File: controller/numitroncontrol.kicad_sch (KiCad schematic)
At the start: 9 parts, among them J0 Screw_Terminal_01x02, J1 Conn_01x06, J2 Conn_01x06, J3 RTC, J4 Screw_Terminal_01x03, U1 LM317_TO-220

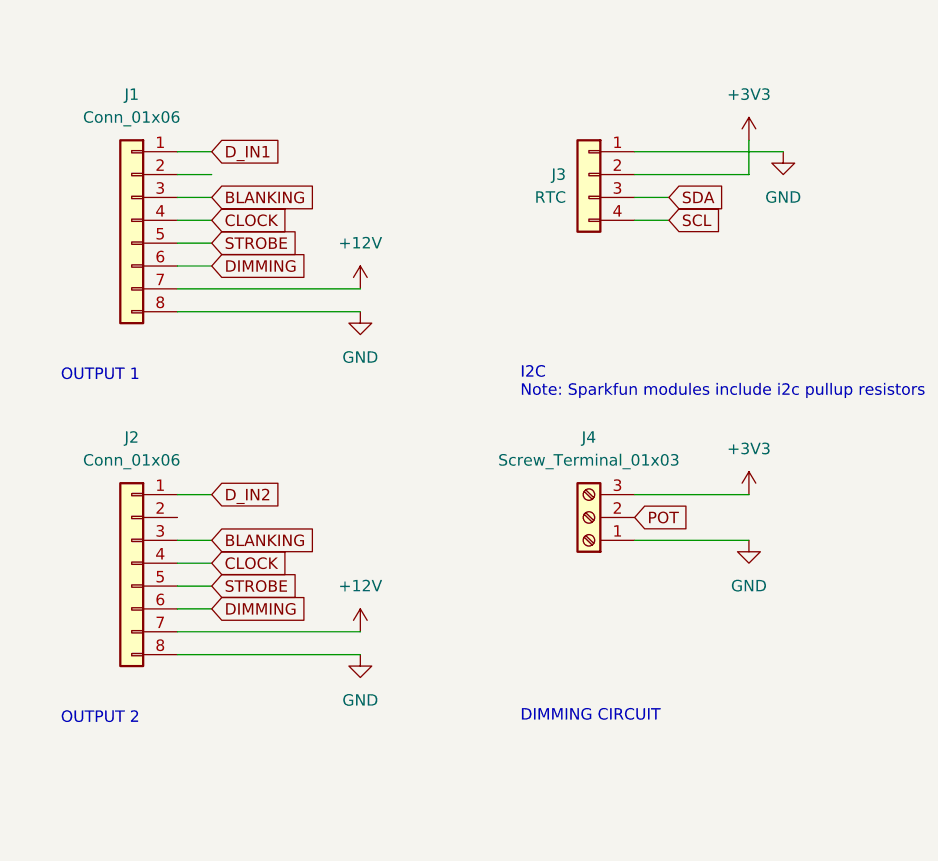
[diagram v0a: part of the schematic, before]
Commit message: Added jumper for control schemes
can have discrete or daisy control of second output on control board
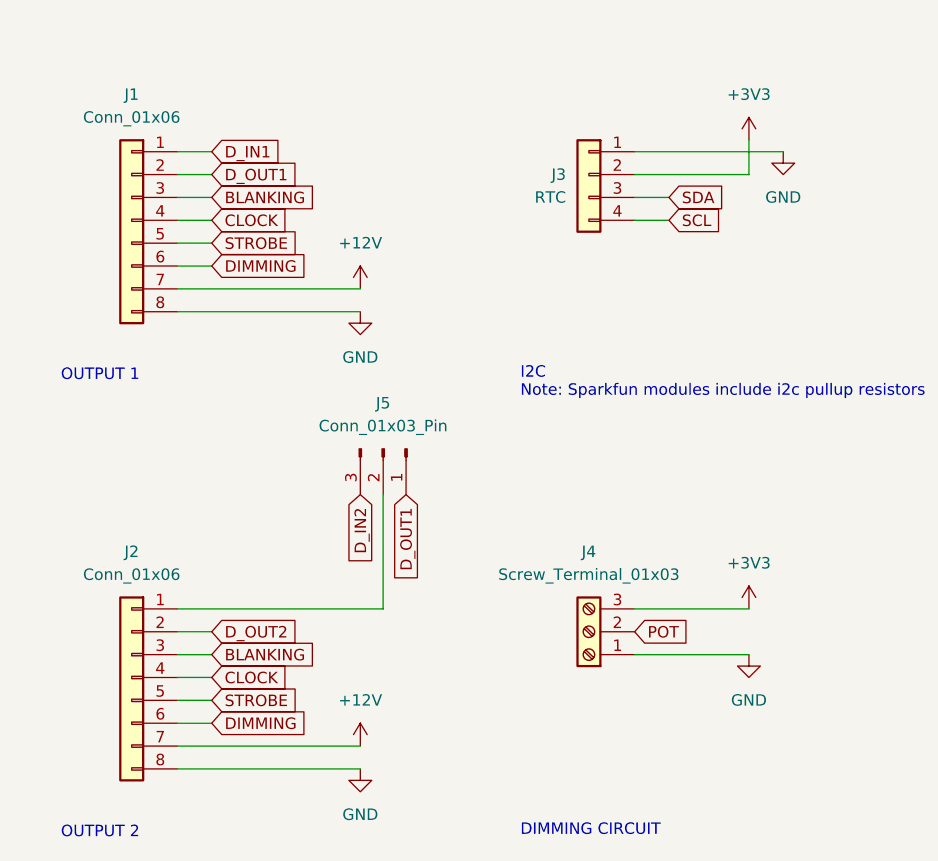
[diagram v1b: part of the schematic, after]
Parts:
- added J5: Conn_01x03_Pin, Connector_PinSocket_2.54mm:PinSocket_1x03_P2.54mm_Vertical, symbol Connector:Conn_01x03_Pin
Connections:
- net D_IN2: now also J5.3 (Pin_3); no longer J2.1 (Pin_1)
- net D_OUT1: now reaches J1.2 (Pin_2)
- net D_OUT1: now also J5.1 (Pin_1)
- net D_OUT2: now reaches J2.2 (Pin_2)
- new net: J2.1 (Pin_1), J5.2 (Pin_2)
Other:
- moved on the sheet: J2, J4

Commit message: control board layout tweaks
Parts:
- J3: symbol Connector_Generic:Conn_01x04 -> Connector:Screw_Terminal_01x04
- J4: footprint TerminalBlock_4Ucon:TerminalBlock_4Ucon_1x03_P3.50mm_Horizontal -> Connector_PinHeader_2.54mm:PinHeader_1x03_P2.54mm_Vertical
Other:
- moved on the sheet: J5
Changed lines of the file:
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@@
+	(wire
+		(pts
+			(xy 31.75 40.64) (xy 25.4 40.64)
+		)
+		(stroke
+			(width 0)
+			(type default)
+		)
+	)
+	(wire
+		(pts
+			(xy 114.3 85.09) (xy 114.3 86.36)
+		)
+		(stroke
+			(width 0)
+			(type default)
+		)
+	)
+	(wire
+		(pts
+			(xy 25.4 38.1) (xy 36.83 38.1)
+		)
+		(stroke
+			(width 0)
+			(type default)
+		)
+	)
+	(wire
+		(pts
+			(xy 48.26 177.8) (xy 48.26 170.18)
+		)
+		(stroke
+			(width 0)
+			(type default)
+		)
+	)
+	(wire
+		(pts
+			(xy 63.5 53.34) (xy 63.5 50.8)
+		)
+		(stroke
+			(width 0)
+			(type default)
+		)
+	)
+	(wire
+		(pts
+			(xy 44.45 50.8) (xy 63.5 50.8)
+		)
+		(stroke
+			(width 0)
+			(type default)
+		)
+	)
+	(wire
+		(pts
+			(xy 25.4 180.34) (xy 29.21 180.34)
+		)
+		(stroke
+			(width 0)
+			(type default)
+		)
+	)
+	(wire
+		(pts
+			(xy 88.9 129.54) (xy 76.2 129.54)
+		)
+		(stroke
+			(width 0)
+			(type default)
+		)
+	)
+	(wire
+		(pts
+			(xy 177.8 63.5) (xy 180.34 63.5)
+		)
+		(stroke
+			(width 0)
+			(type default)
+		)
+	)
+	(wire
+		(pts
+			(xy 123.19 68.58) (xy 127 68.58)
+		)
+		(stroke
+			(width 0)
+			(type default)
+		)
+	)
+	(wire
+		(pts
+			(xy 88.9 125.73) (xy 88.9 129.54)
+		)
+		(stroke
+			(width 0)
+			(type default)
+		)
+	)
+	(wire
+		(pts
+			(xy 25.4 190.5) (xy 29.21 190.5)
+		)
+		(stroke
+			(width 0)
+			(type default)
+		)
+	)
+	(wire
+		(pts
+			(xy 31.75 40.64) (xy 31.75 63.5)
+		)
+		(stroke
+			(width 0)
+			(type default)
+		)
+	)
+	(wire
+		(pts
+			(xy 63.5 63.5) (xy 63.5 60.96)
+		)
+		(stroke
+			(width 0)
+			(type default)
+		)
+	)
+	(wire
+		(pts
+			(xy 114.3 101.6) (xy 114.3 96.52)
+		)
+		(stroke
+			(width 0)
+			(type default)
+		)
+	)
+	(wire
+		(pts
+			(xy 25.4 185.42) (xy 29.21 185.42)
+		)
+		(stroke
+			(width 0)
+			(type default)
+		)
+	)
+	(wire
+		(pts
+			(xy 177.8 66.04) (xy 180.34 66.04)
+		)
+		(stroke
+			(width 0)
+			(type default)
+		)
+	)
+	(wire
+		(pts
+			(xy 25.4 139.7) (xy 29.21 139.7)
+		)
+		(stroke
+			(width 0)
+			(type default)
+		)
+	)
+	(wire
+		(pts
+			(xy 88.9 177.8) (xy 76.2 177.8)
+		)
+		(stroke
+			(width 0)
+			(type default)
+		)
+	)
+	(wire
+		(pts
+			(xy 25.4 129.54) (xy 29.21 129.54)
+		)
+		(stroke
+			(width 0)
+			(type default)
+		)
+	)
+	(wire
+		(pts
+			(xy 106.68 91.44) (xy 127 91.44)
+		)
+		(stroke
+			(width 0)
+			(type default)
+		)
+	)
 	(wire
 		(pts
 			(xy 25.4 177.8) (xy 48.26 177.8)
-		)
-		(stroke
-			(width 0)
-			(type default)
-		)
-	)
-	(wire
-		(pts
-			(xy 31.75 40.64) (xy 25.4 40.64)
-		)
-		(stroke
-			(width 0)
-			(type default)
-		)
-	)
-	(wire
-		(pts
-			(xy 114.3 85.09) (xy 114.3 86.36)
-		)
-		(stroke
-			(width 0)
-			(type default)
-		)
-	)
-	(wire
-		(pts
-			(xy 25.4 38.1) (xy 36.83 38.1)
-		)
-		(stroke
-			(width 0)
-			(type default)
-		)
-	)
-	(wire
-		(pts
-			(xy 48.26 177.8) (xy 48.26 165.1)
-		)
-		(stroke
-			(width 0)
-			(type default)
-		)
-	)
-	(wire
-		(pts
-			(xy 63.5 53.34) (xy 63.5 50.8)
-		)
-		(stroke
-			(width 0)
-			(type default)
-		)
-	)
-	(wire
-		(pts
-			(xy 44.45 50.8) (xy 63.5 50.8)
-		)
-		(stroke
-			(width 0)
-			(type default)
-		)
-	)
-	(wire
-		(pts
-			(xy 25.4 180.34) (xy 29.21 180.34)
-		)
-		(stroke
-			(width 0)
-			(type default)
-		)
-	)
-	(wire
-		(pts
-			(xy 88.9 129.54) (xy 76.2 129.54)
-		)
-		(stroke
-			(width 0)
-			(type default)
-		)
-	)
-	(wire
-		(pts
-			(xy 177.8 63.5) (xy 180.34 63.5)
-		)
-		(stroke
-			(width 0)
-			(type default)
-		)
-	)
-	(wire
-		(pts
-			(xy 123.19 68.58) (xy 127 68.58)
-		)
-		(stroke
-			(width 0)
-			(type default)
-		)
-	)
-	(wire
-		(pts
-			(xy 88.9 125.73) (xy 88.9 129.54)
-		)
-		(stroke
-			(width 0)
-			(type default)
-		)
-	)
-	(wire
-		(pts
-			(xy 25.4 190.5) (xy 29.21 190.5)
-		)
-		(stroke
-			(width 0)
-			(type default)
-		)
-	)
-	(wire
-		(pts
-			(xy 31.75 40.64) (xy 31.75 63.5)
-		)
-		(stroke
-			(width 0)
-			(type default)
-		)
-	)
-	(wire
-		(pts
-			(xy 63.5 63.5) (xy 63.5 60.96)
-		)
-		(stroke
-			(width 0)
-			(type default)
-		)
-	)
-	(wire
-		(pts
-			(xy 114.3 101.6) (xy 114.3 96.52)
-		)
-		(stroke
-			(width 0)
-			(type default)
-		)
-	)
-	(wire
-		(pts
-			(xy 25.4 185.42) (xy 29.21 185.42)
-		)
-		(stroke
-			(width 0)
-			(type default)
-		)
-	)
-	(wire
-		(pts
-			(xy 177.8 66.04) (xy 180.34 66.04)
-		)
-		(stroke
-			(width 0)
-			(type default)
-		)
-	)
-	(wire
-		(pts
-			(xy 25.4 139.7) (xy 29.21 139.7)
-		)
-		(stroke
-			(width 0)
-			(type default)
-		)
-	)
-	(wire
-		(pts
-			(xy 88.9 177.8) (xy 76.2 177.8)
-		)
-		(stroke
-			(width 0)
-			(type default)
-		)
-	)
-	(wire
-		(pts
-			(xy 25.4 129.54) (xy 29.21 129.54)
-		)
-		(stroke
-			(width 0)
-			(type default)
-		)
-	)
-	(wire
-		(pts
-			(xy 106.68 91.44) (xy 127 91.44)
 		)
 		(stroke
@@
 	(global_label "D_OUT1"
 		(shape input)
-		(at 50.8 165.1 270)
+		(at 50.8 170.18 270)
 		(fields_autoplaced yes)
 		(effects
@@
 		)
 		(property "Intersheetrefs" "${INTERSHEET_REFS}"
-			(at 50.8 175.1609 90)
+			(at 50.8 180.2409 90)
 			(effects
 				(font
@@
 	(global_label "D_IN2"
 		(shape input)
-		(at 45.72 165.1 270)
+		(at 45.72 170.18 270)
 		(fields_autoplaced yes)
 		(effects
@@
 		)
 		(property "Intersheetrefs" "${INTERSHEET_REFS}"
-			(at 45.72 173.4676 90)
+			(at 45.72 178.5476 90)
 			(effects
 				(font
@@
 	)
 	(symbol
-		(lib_id "Connector_Generic:Conn_01x04")
+		(lib_id "Connector:Screw_Terminal_01x04")
 		(at 71.12 129.54 0)
 		(mirror y)
@@
 			)
 		)
-		(property "Description" "Generic connector, single row, 01x04, script generated (kicad-library-utils/schlib/autogen/connector/)"
+		(property "Description" "Generic screw terminal, single row, 01x04, script generated (kicad-library-utils/schlib/autogen/connector/)"
 			(at 71.12 129.54 0)
 			(effects
@@
 			)
 		)
-		(property "Footprint" "TerminalBlock_4Ucon:TerminalBlock_4Ucon_1x03_P3.50mm_Horizontal"
+		(property "Footprint" "Connector_PinHeader_2.54mm:PinHeader_1x03_P2.54mm_Vertical"
 			(at 71.12 180.34 0)
 			(effects
@@
 	(symbol
 		(lib_id "Connector:Conn_01x03_Pin")
-		(at 48.26 160.02 270)
+		(at 48.26 165.1 270)
 		(unit 1)
 		(exclude_from_sim no)
@@
 		(fields_autoplaced yes)
 		(property "Reference" "J5"
-			(at 48.26 154.94 90)
+			(at 48.26 160.02 90)
 			(effects
 				(font
@@
 		)
 		(property "Value" "Conn_01x03_Pin"
-			(at 48.26 157.48 90)
+			(at 48.26 162.56 90)
 			(effects
 				(font
@@
 		)
 		(property "Footprint" "Connector_PinSocket_2.54mm:PinSocket_1x03_P2.54mm_Vertical"
-			(at 48.26 160.02 0)
+			(at 48.26 165.1 0)
 			(effects
 				(font
@@
 		)
 		(property "Datasheet" "~"
-			(at 48.26 160.02 0)
+			(at 48.26 165.1 0)
 			(effects
 				(font
@@
 		)
 		(property "Description" "Generic connector, single row, 01x03, script generated"
-			(at 48.26 160.02 0)
-			(effects
-				(font
+			(at 48.26 165.1 0)
+			(effects
+				(font

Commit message: more controller layout updates
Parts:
- J0: footprint TerminalBlock_4Ucon:TerminalBlock_4Ucon_1x02_P3.50mm_Horizontal -> TerminalBlock_TE-Connectivity:TerminalBlock_TE_282834-2_1x02_P2.54mm_Horizontal
- J3: value RTC -> I2C
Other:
- note removed: "Note: Sparkfun modules include i2c pullup resistors"
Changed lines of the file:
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@@
-		)
-	)
-	(text "Note: Sparkfun modules include i2c pullup resistors"
-		(exclude_from_sim no)
-		(at 63.5 153.67 0)
-		(effects
-			(font
-				(size 1.27 1.27)
-			)
-			(justify left)
 		)
 	)
@@
 			)
 		)
-		(property "Value" "RTC"
+		(property "Value" "I2C"
 			(at 68.58 132.0799 0)
 			(effects
@@
 			)
 		)
-		(property "Footprint" "TerminalBlock_4Ucon:TerminalBlock_4Ucon_1x02_P3.50mm_Horizontal"
+		(property "Footprint" "TerminalBlock_TE-Connectivity:TerminalBlock_TE_282834-2_1x02_P2.54mm_Horizontal"
 			(at 20.32 38.1 0)
 			(effects

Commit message: layout updates, gerbers generated
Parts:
- removed J3: I2C, Connector_PinHeader_2.54mm:PinHeader_1x04_P2.54mm_Vertical, symbol Connector:Screw_Terminal_01x04
- removed J4: Screw_Terminal_01x03, Connector_PinHeader_2.54mm:PinHeader_1x03_P2.54mm_Vertical, symbol Connector:Screw_Terminal_01x03
- added J3: Conn_01x04_Pin, symbol Connector:Conn_01x04_Pin
- added J4: Conn_01x03_Pin, symbol Connector:Conn_01x03_Pin
- J5: footprint Connector_PinSocket_2.54mm:PinSocket_1x03_P2.54mm_Vertical -> Connector_PinHeader_2.54mm:PinHeader_1x03_P2.54mm_Vertical
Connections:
- net +3V3: now also J3.2 (Pin_2), J4.1 (Pin_1)
- net GND: now also J3.1 (Pin_1), J4.3 (Pin_3)
- net POT: now also J4.2 (Pin_2)
- net SCL: now also J3.4 (Pin_4)
- net SDA: now also J3.3 (Pin_3)
